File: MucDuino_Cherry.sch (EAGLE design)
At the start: 40 parts, among them Q1 16 MHz, Q2 12 MHz, U1 ATMEGA328, X1 MINI-USB-UX60-MB-5ST

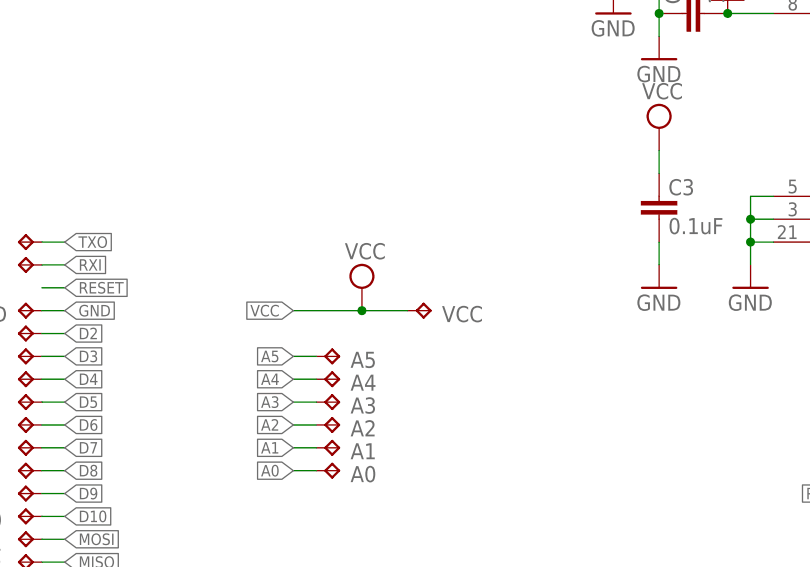
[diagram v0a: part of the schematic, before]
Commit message: Ad Cherry variant of MucDuino, fix Banana Version, ad USB Uart Datascheet
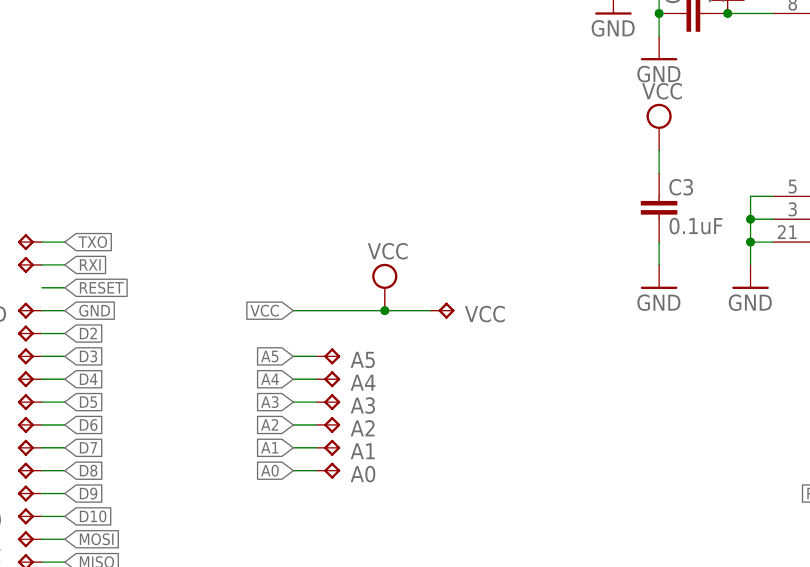
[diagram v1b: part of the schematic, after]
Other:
- moved on the sheet: VCC
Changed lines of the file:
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@@
 <attribute name="TP_SIGNAL_NAME" x="64.77" y="92.71" size="1.778" layer="97" rot="R90"/>
 </instance>
-<instance part="VCC" gate="G$1" x="109.22" y="91.44" smashed="yes" rot="R270">
-<attribute name="NAME" x="110.49" y="90.17" size="1.778" layer="95"/>
-<attribute name="TP_SIGNAL_NAME" x="107.95" y="90.17" size="1.778" layer="97" rot="R270"/>
+<instance part="VCC" gate="G$1" x="111.76" y="91.44" smashed="yes" rot="R270">
+<attribute name="NAME" x="113.03" y="90.17" size="1.778" layer="95"/>
+<attribute name="TP_SIGNAL_NAME" x="110.49" y="90.17" size="1.778" layer="97" rot="R270"/>
 </instance>
 <instance part="C4" gate="G$1" x="137.16" y="129.54" smashed="yes" rot="R270">
@@
 <instance part="SUPPLY5" gate="G$1" x="50.8" y="139.7"/>
 <instance part="SUPPLY6" gate="G$1" x="12.7" y="177.8"/>
-<instance part="SUPPLY7" gate="G$1" x="101.6" y="93.98"/>
+<instance part="SUPPLY7" gate="G$1" x="104.14" y="93.98"/>
 </instances>
 <busses>
@@
 </segment>
 <segment>
-<wire x1="106.68" y1="91.44" x2="101.6" y2="91.44" width="0.1524" layer="91"/>
+<wire x1="109.22" y1="91.44" x2="104.14" y2="91.44" width="0.1524" layer="91"/>
 <label x="93.98" y="91.44" size="1.27" layer="95" rot="R180" xref="yes"/>
 <pinref part="VCC" gate="G$1" pin="TP"/>
 <pinref part="SUPPLY7" gate="G$1" pin="VCC"/>
-<wire x1="101.6" y1="91.44" x2="93.98" y2="91.44" width="0.1524" layer="91"/>
-<junction x="101.6" y="91.44"/>
-</segment>
-<segment>
+<wire x1="104.14" y1="91.44" x2="93.98" y2="91.44" width="0.1524" layer="91"/>
+<junction x="104.14" y="91.44"/>
+</segment>
+<segment>
